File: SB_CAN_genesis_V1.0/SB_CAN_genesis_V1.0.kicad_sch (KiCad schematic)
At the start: 6 parts, among them J2 USB_B_Micro, U1 STM32F072CBUx, U2 TMC2209-LA-T, U3 SN65HVD230DR

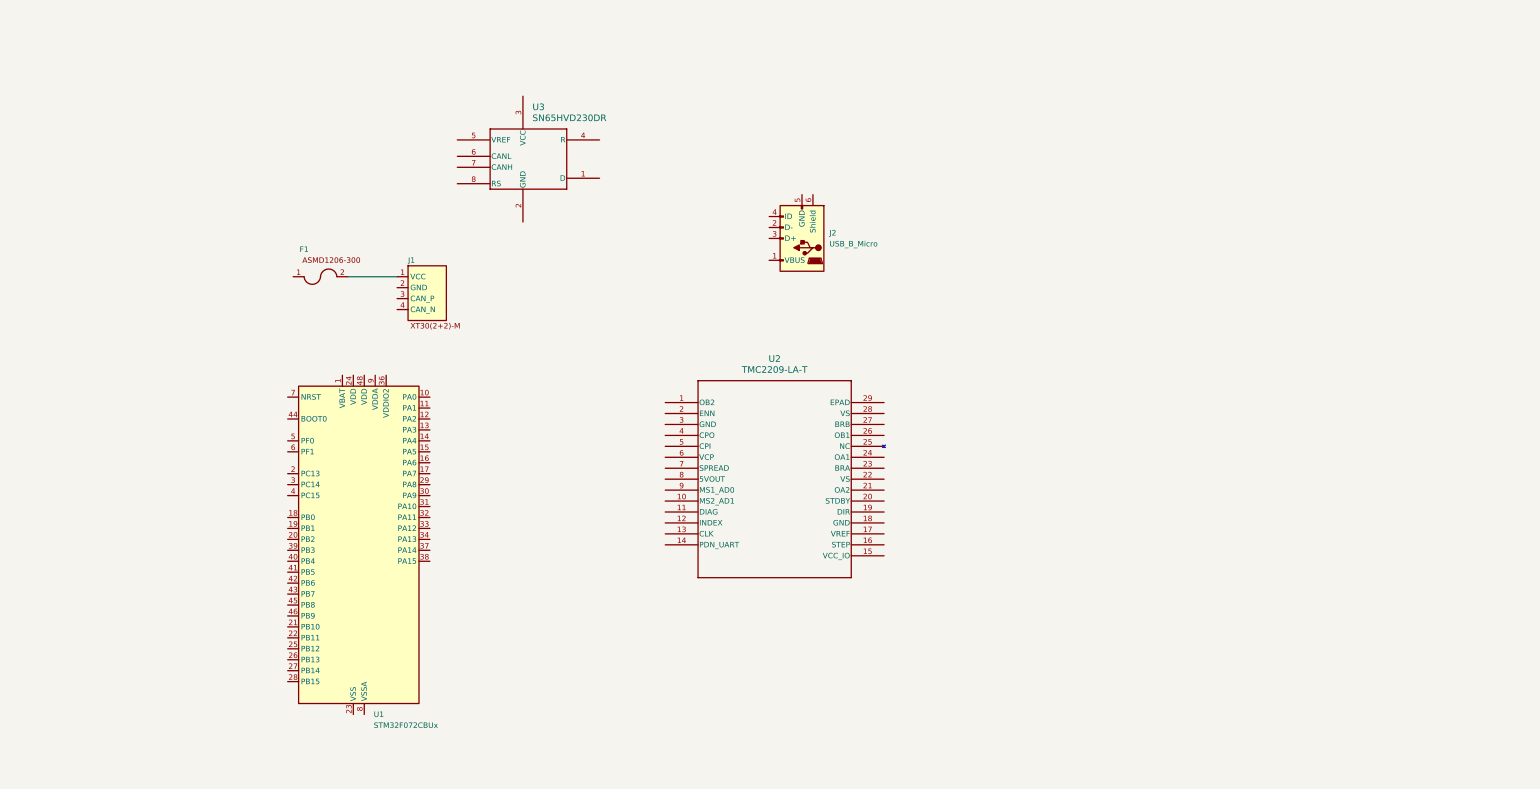
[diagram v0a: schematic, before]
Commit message: Add new parts for the board
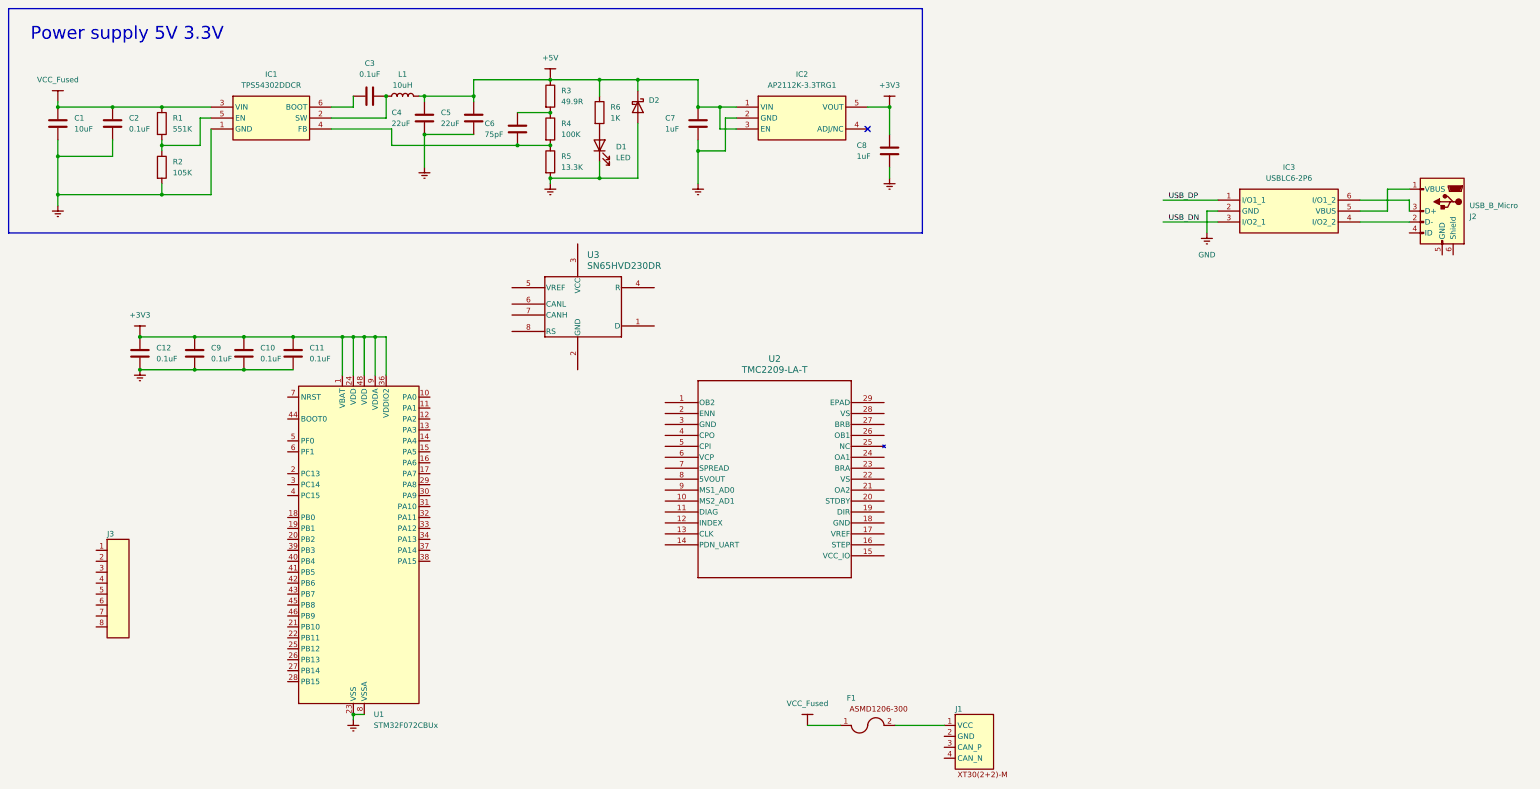
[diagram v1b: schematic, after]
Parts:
- added C1: 10uF, Capacitor_SMD:C_0201_0603Metric, symbol Device:C
- added C10, C11, C12, C2, C3, C9: 0.1uF, Capacitor_SMD:C_0201_0603Metric, symbol Device:C
- added C4, C5: 22uF, Capacitor_SMD:C_0201_0603Metric, symbol Device:C
- added C6: 75pF, Capacitor_SMD:C_0201_0603Metric, symbol Device:C
- added C7, C8: 1uF, Capacitor_SMD:C_0201_0603Metric, symbol Device:C
- added D1: LED, LED_SMD:LED_0402_1005Metric, symbol Device:LED
- added D2: D_Schottky, Diode_SMD:D_0201_0603Metric, symbol Device:D_Schottky
- added IC1: TPS54302DDCR, SB_CAN_genesis_V1.0_lib:SOT95P280X110-6N, symbol SB_CAN_genesis_V1.0_lib:TPS54302DDCR
- added IC2: AP2112K-3.3TRG1, SOT95P282X130-5N, symbol SB_CAN_genesis_V1.0_lib:AP2112K-3.3TRG1
- added IC3: USBLC6-2P6, SB_CAN_genesis_V1.0_lib:USBLC62P6, symbol SB_CAN_genesis_V1.0_lib:USBLC6-2P6
- added J3: ~, SB_CAN_genesis_V1.0_lib:1.27mm 4x2 header F, symbol SB_CAN_genesis_V1.0_lib:1.27mm_Header_2x4
- added L1: 10uH, Inductor_SMD:L_0603_1608Metric, symbol Device:L
- added R1: 551K, Resistor_SMD:R_0201_0603Metric, symbol Device:R
- added R2: 105K, Resistor_SMD:R_0201_0603Metric, symbol Device:R
- added R3: 49.9R, Resistor_SMD:R_0201_0603Metric, symbol Device:R
- added R4: 100K, Resistor_SMD:R_0201_0603Metric, symbol Device:R
- added R5: 13.3K, Resistor_SMD:R_0201_0603Metric, symbol Device:R
- added R6: 1K, Resistor_SMD:R_0201_0603Metric, symbol Device:R
- F1: footprint (none) -> Resistor_SMD:R_1206_3216Metric
- U2: footprint SB_CAN_genesis_V1.0_lib:QFN28_5X5_3X8_EPAD_TRI -> SB_CAN_genesis_V1.0_lib:QFN-28-1EP_5x5mm_P0.5mm_EP3.75x3.75mm_ThermalVias
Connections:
- net VCC: now reaches F1.1
- net VCC: now also U1.1 (VBAT), U1.24 (VDD), U1.36 (VDDIO2), U1.48 (VDD), U1.9 (VDDA), C1.1, C10.1, C11.1, C12.1, C2.1, C4.2, C5.2, C7.2, C8.2, C9.1, D2.1 (K), IC1.3 (VIN), IC2.1 (VIN), IC2.3 (EN), IC2.5 (VOUT), L1.2, R1.1, R3.1, R6.1
- net GNDREF: now reaches U1.23 (VSS), U1.35 (VSS), U1.47 (VSS), U1.49 (VSS)
- net GNDREF: now also U1.8 (VSSA), C1.2, C10.2, C11.2, C12.2, C2.2, C4.1, C5.1, C7.1, C8.1, C9.2, D1.1 (K), D2.2 (A), IC1.1 (GND), IC2.2 (GND), IC3.2 (GND), R2.2, R5.2
- net at J2.1 (VBUS): now also IC3.5 (VBUS)
- net at J2.2 (D-): now also IC3.4 (I/O2_2)
- net at J2.3 (D+): now also IC3.6 (I/O1_2)
- new net: D1.2 (A), R6.2
- new net: C6.2, R3.2, R4.1
- new net: C6.1, IC1.4 (FB), R4.2, R5.1
- new net: IC1.5 (EN), R1.2, R2.1
- new net: C3.2, IC1.2 (SW), L1.1
- new net: C3.1, IC1.6 (BOOT)
- new net USB_DN: IC3.3 (I/O2_1)
- new net USB_DP: IC3.1 (I/O1_1)
- no-connect marks 0 -> 1
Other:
- note added: "Power supply 5V 3.3V"
- moved on the sheet: F1, J1, J2, U3
